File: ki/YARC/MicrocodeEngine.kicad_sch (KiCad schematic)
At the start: 12 parts

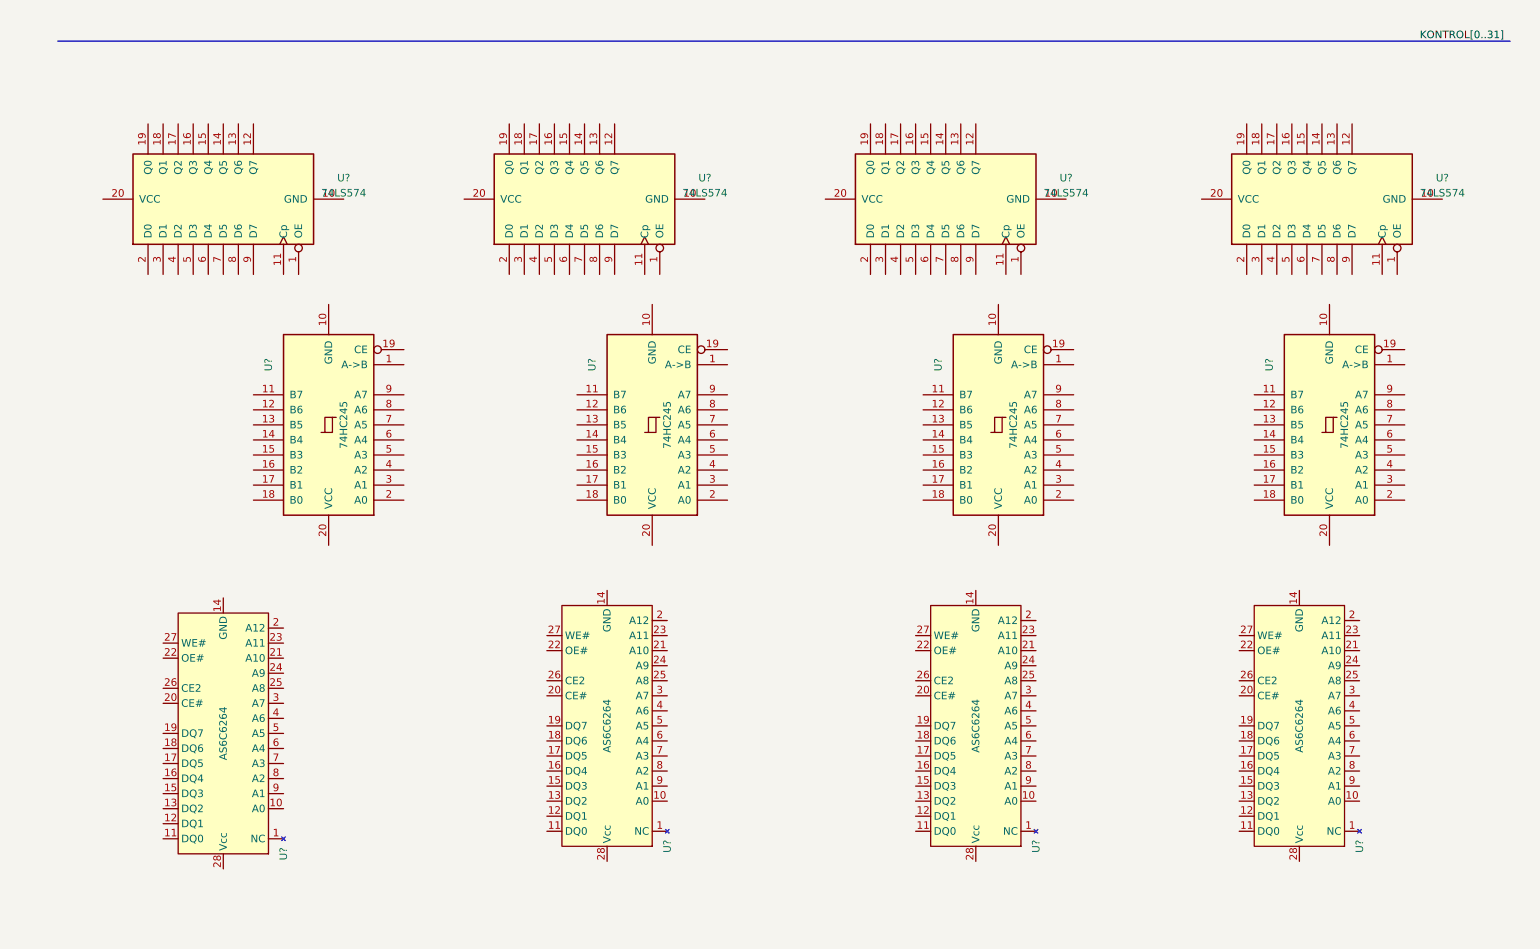
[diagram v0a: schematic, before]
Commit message: Update README and docs. Progress on KiCad ucode schematic. Moved yasm code.
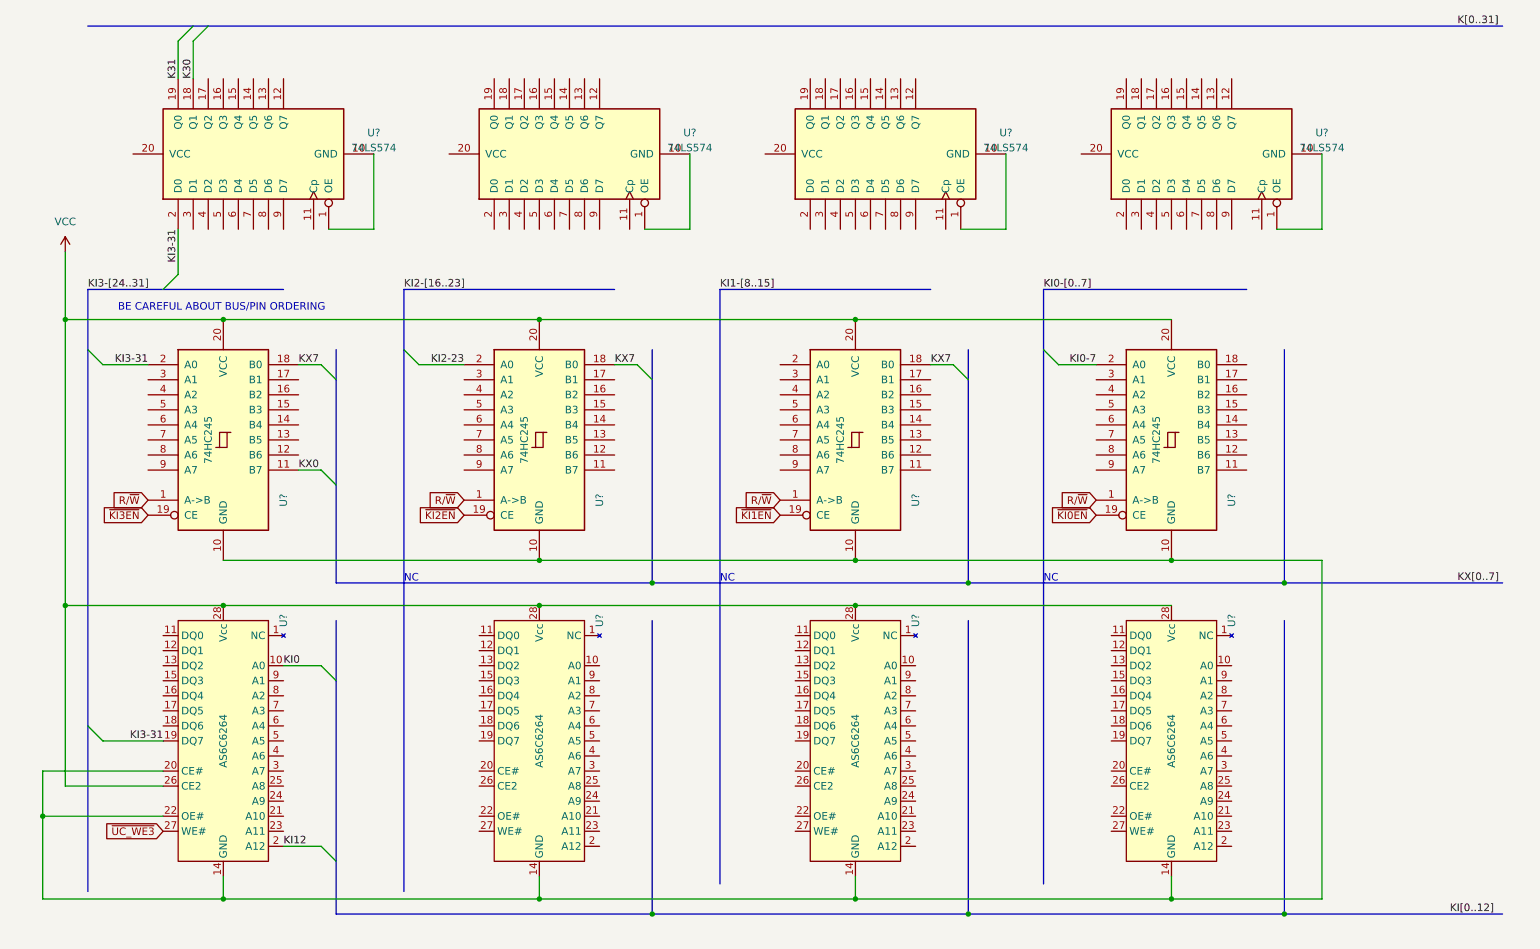
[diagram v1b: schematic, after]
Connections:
- net at U?.1 (OE): now also U?.10 (GND) (x4)
- net at U?.14 (GND): now also U?.10 (GND), U?.10 (GND), U?.10 (GND), U?.10 (GND), U?.14 (GND), U?.14 (GND), U?.14 (GND), U?.20 (CE#), U?.22 (OE#)
- net VCC: now reaches U?.28 (Vcc)
- net VCC: now also U?.20 (VCC), U?.20 (VCC), U?.20 (VCC), U?.20 (VCC), U?.26 (CE2), U?.28 (Vcc), U?.28 (Vcc), U?.28 (Vcc)
- net R/~{W}: now reaches U?.1 (A->B)
- net R/~{W}: now also U?.1 (A->B), U?.1 (A->B), U?.1 (A->B)
- net KX0: now reaches U?.11 (B7)
- net KX7: now reaches U?.18 (B0)
- net KX7: now also U?.18 (B0), U?.18 (B0)
- net ~{KI3EN}: now reaches U?.19 (CE)
- net KI3-31: now reaches U?.2 (A0)
- net KI3-31: now also U?.19 (DQ7), U?.2 (D0)
- net KI0: now reaches U?.10 (A0)
- net KI12: now reaches U?.2 (A12)
- net ~{UC_WE3}: now reaches U?.27 (WE#)
- net K30: now reaches U?.18 (Q1)
- net K31: now reaches U?.19 (Q0)
- net ~{KI2EN}: now reaches U?.19 (CE)
- net KI2-23: now reaches U?.2 (A0)
- net ~{KI0EN}: now reaches U?.19 (CE)
- net KI0-7: now reaches U?.2 (A0)
- net ~{KI1EN}: now reaches U?.19 (CE)
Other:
- note added: "BE CAREFUL ABOUT BUS/PIN ORDERING"
- note added: "NC"
- moved on the sheet: U?

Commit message: Significant progress on microcode schematic. Minor improvements to MemorySystem.md.
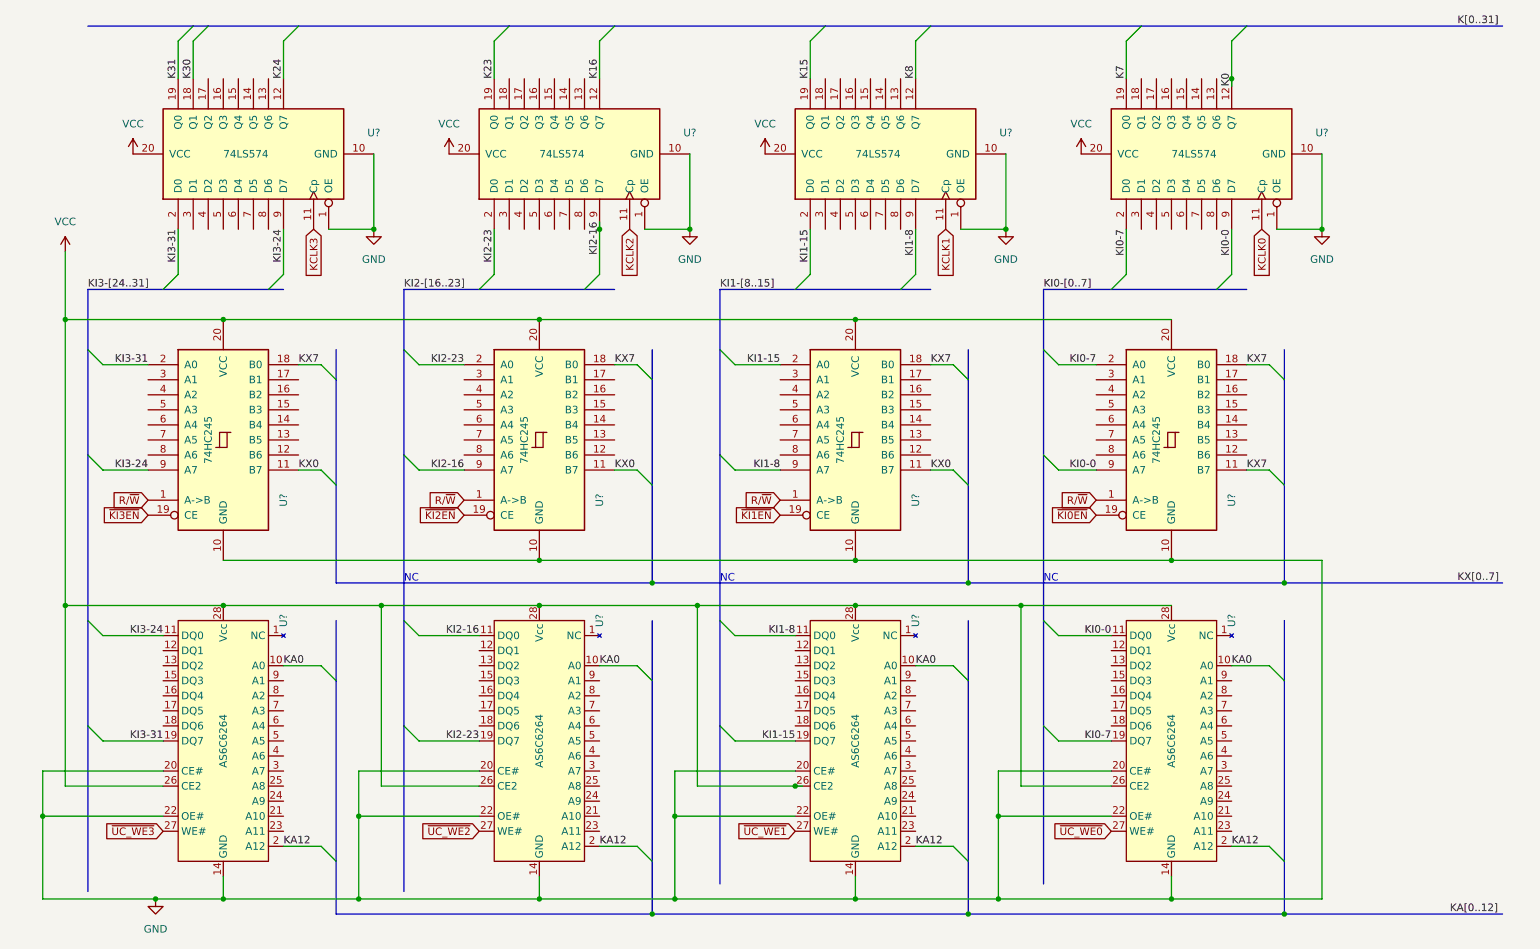
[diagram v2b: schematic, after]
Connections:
- net KI0 is gone; now on net KA0: U?.10 (A0)
- net KI12 is gone; now on net KA12: U?.2 (A12)
- net KI0-7: now also U?.19 (DQ7), U?.2 (D0)
- net KI2-23: now also U?.19 (DQ7), U?.2 (D0)
- net KX0: now also U?.11 (B7), U?.11 (B7)
- net KX7: now also U?.11 (B7), U?.18 (B0)
- net VCC: now also U?.20 (VCC), U?.20 (VCC), U?.20 (VCC), U?.20 (VCC), U?.26 (CE2), U?.26 (CE2), U?.26 (CE2)
- net GND: now reaches U?.1 (OE), U?.10 (GND)
- net GND: now also U?.1 (OE), U?.1 (OE), U?.1 (OE), U?.10 (GND), U?.10 (GND), U?.10 (GND), U?.10 (GND), U?.10 (GND), U?.10 (GND), U?.10 (GND), U?.14 (GND), U?.14 (GND), U?.14 (GND), U?.14 (GND), U?.20 (CE#), U?.20 (CE#), U?.20 (CE#), U?.20 (CE#), U?.22 (OE#), U?.22 (OE#), U?.22 (OE#), U?.22 (OE#)
- net KCLK2: now reaches U?.11 (Cp)
- net K16: now reaches U?.12 (Q7)
- net K23: now reaches U?.19 (Q0)
- net KI2-16: now reaches U?.9 (D7)
- net KI2-16: now also U?.11 (DQ0), U?.9 (A7)
- net KA0: now reaches U?.10 (A0)
- net KA0: now also U?.10 (A0), U?.10 (A0)
- net KA12: now reaches U?.2 (A12)
- net KA12: now also U?.2 (A12), U?.2 (A12)
- net ~{UC_WE2}: now reaches U?.27 (WE#)
- net KI3-24: now reaches U?.9 (A7)
- net KI3-24: now also U?.11 (DQ0), U?.9 (D7)
- net KCLK0: now reaches U?.11 (Cp)
- net K0: now reaches U?.12 (Q7)
- net K7: now reaches U?.19 (Q0)
- net KI0-0: now reaches U?.9 (D7)
- net KI0-0: now also U?.11 (DQ0), U?.9 (A7)
- net KCLK3: now reaches U?.11 (Cp)
- net K24: now reaches U?.12 (Q7)
- net KCLK1: now reaches U?.11 (Cp)
- net K8: now reaches U?.12 (Q7)
- net K15: now reaches U?.19 (Q0)
- net KI1-15: now reaches U?.2 (D0)
- net KI1-15: now also U?.19 (DQ7), U?.2 (A0)
- net KI1-8: now reaches U?.9 (D7)
- net KI1-8: now also U?.11 (DQ0), U?.9 (A7)
- net ~{UC_WE1}: now reaches U?.27 (WE#)
- net ~{UC_WE0}: now reaches U?.27 (WE#)
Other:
- note removed: "BE CAREFUL ABOUT BUS/PIN ORDERING"

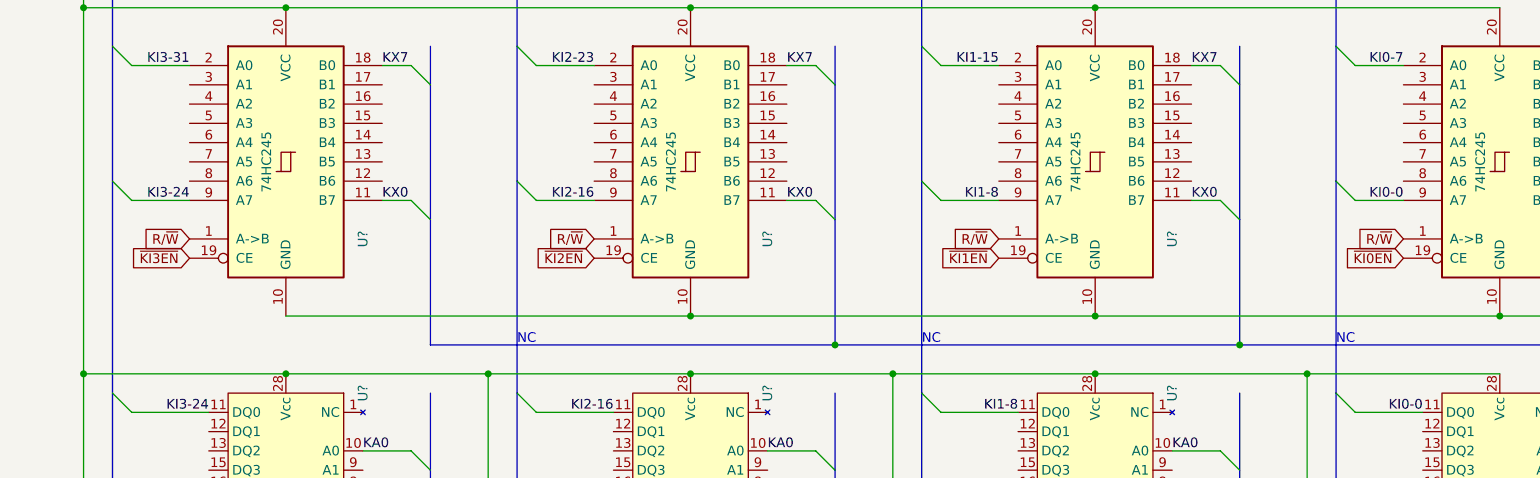
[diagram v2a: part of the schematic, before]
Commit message: Fixing wiring diagram and implement writeToK()
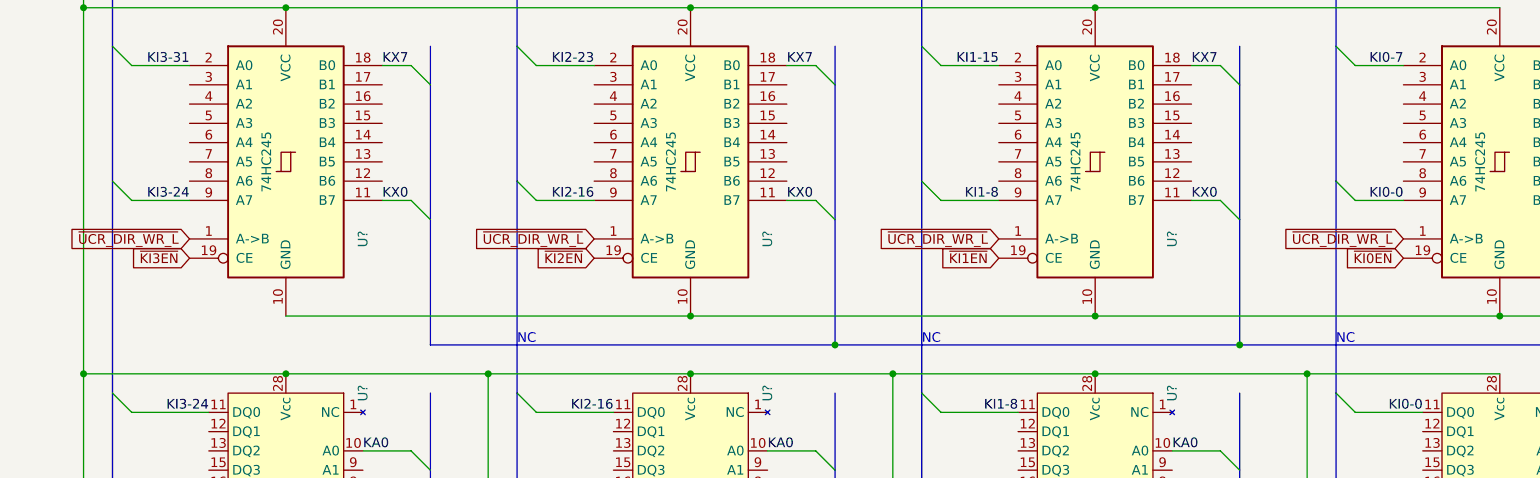
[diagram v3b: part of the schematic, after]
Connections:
- net R/~{W} renamed ~{UCR_DIR_WR_L}
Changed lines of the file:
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@@
     (effects (font (size 1.27 1.27)) (justify left bottom))
   )
-  (global_label "R{slash}~{W}" (shape input) (at 86.36 97.79 180) (fields_autoplaced)
+  (global_label "~{UCR_DIR_WR_L}" (shape input) (at 33.02 97.79 180) (fields_autoplaced)
     (effects (font (size 1.27 1.27)) (justify right))
-    (property "Intersheet References" "${INTERSHEET_REFS}" (id 0) (at 79.895 97.7106 0)
+    (property "Intersheet References" "${INTERSHEET_REFS}" (id 0) (at 16.9393 97.7106 0)
       (effects (font (size 1.27 1.27)) (justify right) hide)
     )
   )
-  (global_label "R{slash}~{W}" (shape input) (at 33.02 97.79 180) (fields_autoplaced)
+  (global_label "~{UCR_DIR_WR_L}" (shape input) (at 193.04 97.79 180) (fields_autoplaced)
     (effects (font (size 1.27 1.27)) (justify right))
-    (property "Intersheet References" "${INTERSHEET_REFS}" (id 0) (at 26.555 97.7106 0)
+    (property "Intersheet References" "${INTERSHEET_REFS}" (id 0) (at 176.9593 97.7106 0)
+      (effects (font (size 1.27 1.27)) (justify right) hide)
+    )
+  )
+  (global_label "~{UCR_DIR_WR_L}" (shape input) (at 139.7 97.79 180) (fields_autoplaced)
+    (effects (font (size 1.27 1.27)) (justify right))
+    (property "Intersheet References" "${INTERSHEET_REFS}" (id 0) (at 123.6193 97.7106 0)
       (effects (font (size 1.27 1.27)) (justify right) hide)
     )
@@
     )
   )
-  (global_label "R{slash}~{W}" (shape input) (at 193.04 97.79 180) (fields_autoplaced)
-    (effects (font (size 1.27 1.27)) (justify right))
-    (property "Intersheet References" "${INTERSHEET_REFS}" (id 0) (at 186.575 97.7106 0)
-      (effects (font (size 1.27 1.27)) (justify right) hide)
-    )
-  )
   (global_label "KCLK0" (shape input) (at 220.98 52.07 270) (fields_autoplaced)
     (effects (font (size 1.27 1.27)) (justify right))
     (property "Intersheet References" "${INTERSHEET_REFS}" (id 0) (at 221.0594 60.5307 90)
-      (effects (font (size 1.27 1.27)) (justify right) hide)
-    )
-  )
-  (global_label "R{slash}~{W}" (shape input) (at 139.7 97.79 180) (fields_autoplaced)
-    (effects (font (size 1.27 1.27)) (justify right))
-    (property "Intersheet References" "${INTERSHEET_REFS}" (id 0) (at 133.235 97.7106 0)
       (effects (font (size 1.27 1.27)) (justify right) hide)
     )
@@
       (effects (font (size 1.27 1.27)) (justify right) hide)
     )
+  )
+  (global_label "~{UCR_DIR_WR_L}" (shape input) (at 86.36 97.79 180) (fields_autoplaced)
+    (effects (font (size 1.27 1.27)) (justify right))
+    (property "Intersheet References" "${INTERSHEET_REFS}" (id 0) (at 70.2793 97.7106 0)
+      (effects (font (size 1.27 1.27)) (justify right) hide)
+    )
